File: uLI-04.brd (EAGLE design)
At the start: 57 x 38.5 mm, 38 parts, among them IC1 PIC18F14K50-I/SS, IC2 ADM2483, IC4 78L05F, J1 PICPROG2-V, J5 WEBP6-4, J6 WEBP6-4, J7 WEBP6-4, Q1 12.00 MHz, T1 IRF7306, X1 MINI-USB_SHIELD4P-USB-SPEC, X2 ARK1550/2_S

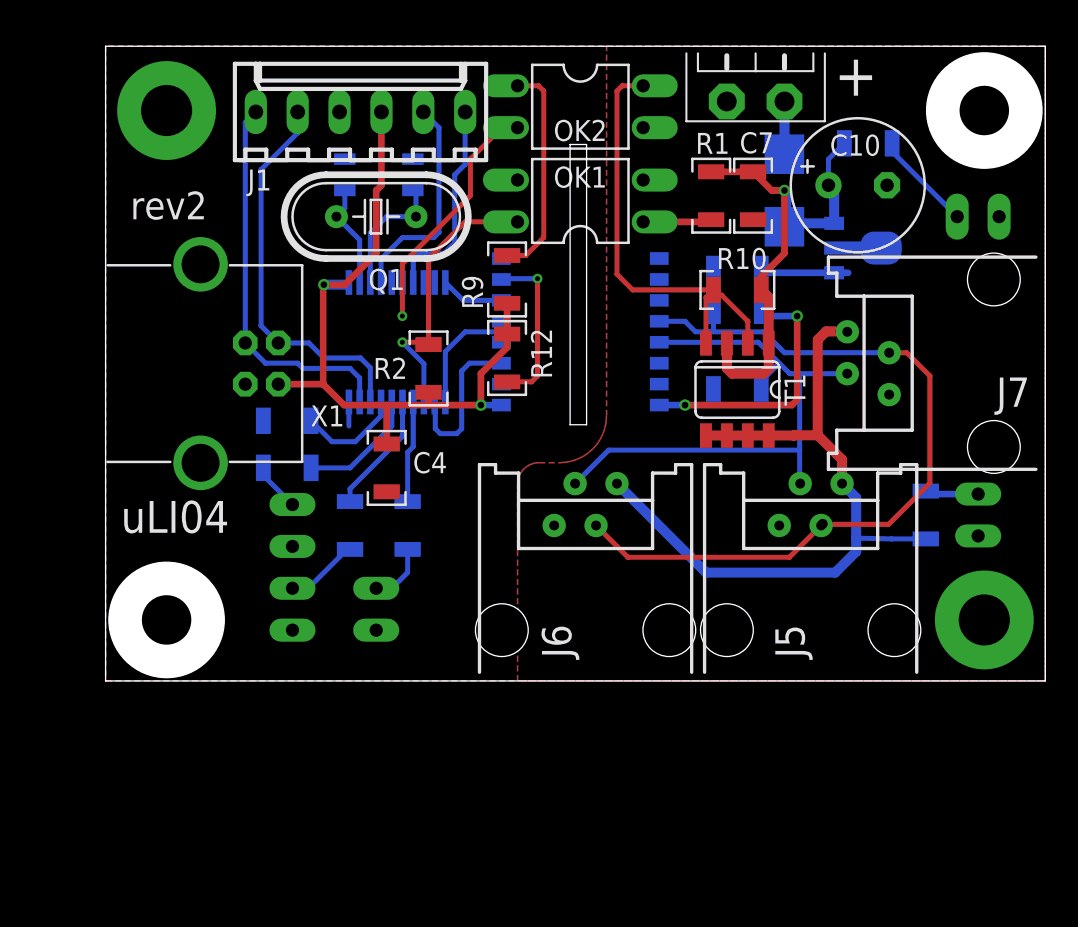
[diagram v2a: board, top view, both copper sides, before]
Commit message: Omezeni proudovych razu - schema
Pridan na schema rezistor a zmensen kondenzator pred stabilizator.
Editovano jen schema. Deska neupravena.
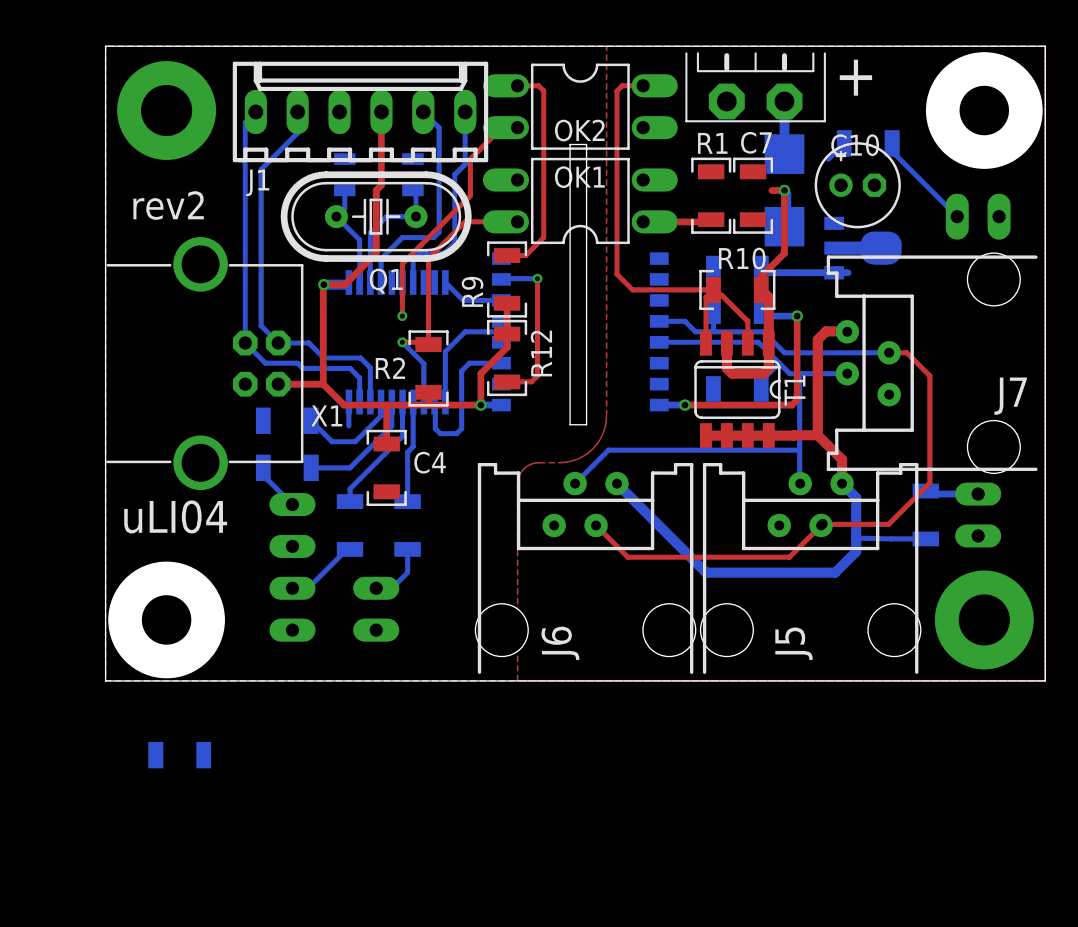
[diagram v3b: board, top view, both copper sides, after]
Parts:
- added R13: 22R, rcl:R1206
- C10: value 220u/35V -> 10u/35V; device rcl:E3,5-8 -> rcl:E2-5
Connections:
- new net N$10: C10.+, C7.1, IC4.3, R13.1
- net +12V: now also R13.2; no longer C10.+, C7.1, IC4.3
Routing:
- net +12V: track 31.4 -> 20.4 mm
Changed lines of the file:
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@@
 <grid distance="0.5" unitdist="mm" unit="mm" style="dots" multiple="2" display="no" altdistance="0.1" altunitdist="mm" altunit="mm"/>
 <layers>
-<layer number="1" name="Top" color="3" fill="1" visible="yes" active="yes"/>
+<layer number="1" name="Top" color="3" fill="1" visible="no" active="yes"/>
 <layer number="2" name="Route2" color="1" fill="3" visible="no" active="no"/>
 <layer number="3" name="Route3" color="4" fill="3" visible="no" active="no"/>
@@
 <layer number="19" name="Unrouted" color="6" fill="1" visible="yes" active="yes"/>
 <layer number="20" name="Dimension" color="15" fill="1" visible="yes" active="yes"/>
-<layer number="21" name="tPlace" color="7" fill="1" visible="yes" active="yes"/>
+<layer number="21" name="tPlace" color="7" fill="1" visible="no" active="yes"/>
 <layer number="22" name="bPlace" color="7" fill="1" visible="yes" active="yes"/>
-<layer number="23" name="tOrigins" color="15" fill="1" visible="yes" active="yes"/>
+<layer number="23" name="tOrigins" color="15" fill="1" visible="no" active="yes"/>
 <layer number="24" name="bOrigins" color="15" fill="1" visible="yes" active="yes"/>
 <layer number="25" name="tNames" color="7" fill="1" visible="no" active="yes"/>
@@
 <layer number="44" name="Drills" color="7" fill="1" visible="no" active="yes"/>
 <layer number="45" name="Holes" color="7" fill="1" visible="no" active="yes"/>
-<layer number="46" name="Milling" color="3" fill="1" visible="yes" active="yes"/>
+<layer number="46" name="Milling" color="3" fill="1" visible="no" active="yes"/>
 <layer number="47" name="Measures" color="7" fill="1" visible="no" active="yes"/>
 <layer number="48" name="Document" color="7" fill="1" visible="no" active="yes"/>
-<layer number="49" name="Reference" color="7" fill="1" visible="yes" active="yes"/>
+<layer number="49" name="Reference" color="7" fill="1" visible="no" active="yes"/>
 <layer number="50" name="dxf" color="7" fill="1" visible="no" active="no"/>
-<layer number="51" name="tDocu" color="7" fill="1" visible="yes" active="yes"/>
+<layer number="51" name="tDocu" color="7" fill="1" visible="no" active="yes"/>
 <layer number="52" name="bDocu" color="7" fill="1" visible="yes" active="yes"/>
 <layer number="53" name="tGND_GNDA" color="7" fill="9" visible="no" active="no"/>
@@
 <element name="R10" library="rcl" package="R1206" value="100k" x="40.3225" y="25.7175"/>
 <element name="T1" library="transistor-fet" package="SO08-IRF" value="IRF7306" x="40.3225" y="19.685" rot="R180"/>
-<element name="C10" library="rcl" package="E3,5-8" value="220u/35V" x="47.625" y="32.0675" smashed="yes">
+<element name="C10" library="rcl" package="E2-5" value="10u/35V" x="47.625" y="32.0675" smashed="yes">
 <attribute name="NAME" x="45.927" y="33.8615" size="1.27" layer="25" ratio="10"/>
 <attribute name="VALUE" x="45.339" y="34.0195" size="1.27" layer="27" ratio="10"/>
@@
 <attribute name="VALUE" x="28.8925" y="20.32" size="1.27" layer="27" font="vector" ratio="15" rot="R90"/>
 </element>
+<element name="R13" library="rcl" package="R1206" value="22R" x="6.5" y="-2.5" rot="MR180"/>
 </elements>
 <signals>
@@
 </signal>
 <signal name="+12V" class="1">
-<contactref element="IC4" pad="3"/>
-<contactref element="C7" pad="1"/>
 <contactref element="R1" pad="2"/>
 <contactref element="R8" pad="2"/>
@@
 <contactref element="T1" pad="3"/>
 <contactref element="T1" pad="1"/>
-<contactref element="C10" pad="+"/>
-<wire x1="46.1925" y1="29.7565" x2="43.3865" y2="29.7565" width="0.6096" layer="16"/>
 <wire x1="43.3865" y1="29.7565" x2="43.18" y2="29.55" width="0.6096" layer="16"/>
-<wire x1="46.1925" y1="29.7565" x2="46.1925" y2="31.722" width="0.6096" layer="16"/>
-<wire x1="46.1925" y1="31.722" x2="45.847" y2="32.0675" width="0.6096" layer="16"/>
 <wire x1="39.6875" y1="22.485" x2="39.6875" y2="20.955" width="0.6096" layer="1"/>
 <wire x1="39.6875" y1="20.955" x2="40.005" y2="20.6375" width="0.6096" layer="1"/>
@@
 <via x="43.18" y="31.75" extent="1-16" drill="0.4"/>
 <wire x1="43.18" y1="31.75" x2="42.4075" y2="31.75" width="0.4064" layer="1"/>
-<wire x1="42.4075" y1="31.75" x2="41.275" y2="32.8825" width="0.4064" layer="1"/>
 <wire x1="41.7725" y1="25.7175" x2="41.7725" y2="26.5325" width="0.4064" layer="1"/>
 <wire x1="41.7725" y1="26.5325" x2="43.18" y2="27.94" width="0.4064" layer="1"/>
 <wire x1="43.18" y1="27.94" x2="43.18" y2="31.75" width="0.4064" layer="1"/>
-<wire x1="38.735" y1="32.8825" x2="41.275" y2="32.8825" width="0.4064" layer="1"/>
-<wire x1="45.847" y1="32.0675" x2="45.847" y2="33.6445" width="0.3048" layer="16"/>
 <wire x1="45.847" y1="33.6445" x2="46.81" y2="34.6075" width="0.3048" layer="16"/>
+<contactref element="R13" pad="2"/>
+<wire x1="43.3865" y1="31.5435" x2="45.847" y2="33.6445" width="0" layer="19" extent="16-16"/>
+<wire x1="38.735" y1="32.8825" x2="42.4075" y2="31.75" width="0" layer="19" extent="1-1"/>
+<wire x1="7.95" y1="-2.5" x2="39.6875" y2="20.955" width="0" layer="19" extent="1-16"/>
 </signal>
 <signal name="XTAL2">
@@
 <wire x1="22" y1="18.8775" x2="21.96" y2="18.9175" width="0.3048" layer="16"/>
 </signal>
+<signal name="N$10" class="1">
+<contactref element="C10" pad="+"/>
+<contactref element="R13" pad="1"/>
+<contactref element="C7" pad="1"/>
+<contactref element="IC4" pad="3"/>
+<wire x1="46.1925" y1="29.7565" x2="46.609" y2="32.0675" width="0" layer="19" extent="16-16"/>
+<wire x1="41.275" y1="32.8825" x2="46.609" y2="32.0675" width="0" layer="19" extent="1-1"/>
+<wire x1="5.05" y1="-2.5" x2="41.275" y2="32.8825" width="0" layer="19" extent="1-16"/>
+</signal>
 </signals>

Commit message: Pridan brown-out reset pro PV pin
Jen schema.
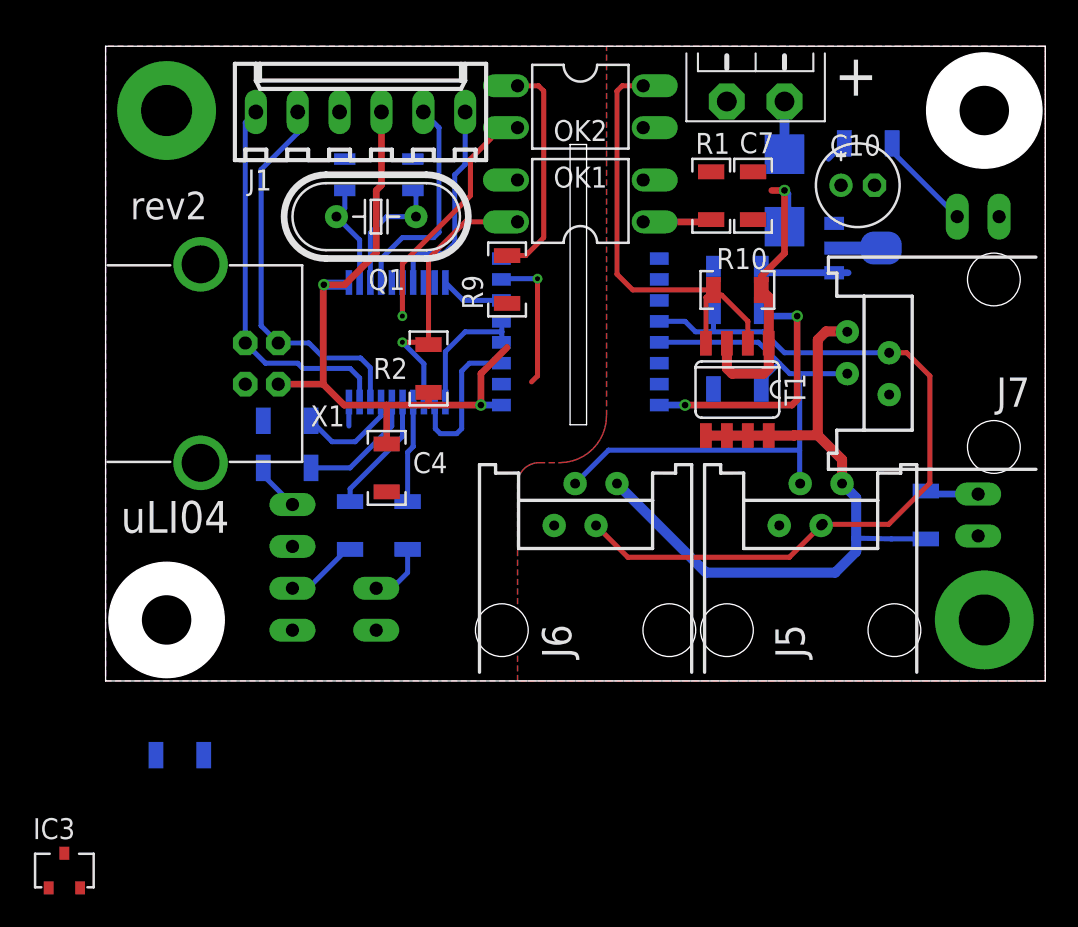
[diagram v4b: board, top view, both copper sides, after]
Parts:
- removed R12: OR, rcl:R1206
- added IC3: MCP130T, my:SOT23
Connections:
- removed net N$8: IC2.7, R12.1
- new net PV: IC2.7, IC3.1
- net GND: now also IC3.3
- net VDD: now also IC3.2; no longer R12.2
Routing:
- net N$8: track 10.1 -> 0.00 mm, vias 1 -> 0
- net PV: track 0.00 -> 8.62 mm, vias 0 -> 1
- net VDD: track 44.3 -> 41.6 mm
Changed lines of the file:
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@@
 <grid distance="0.5" unitdist="mm" unit="mm" style="dots" multiple="2" display="no" altdistance="0.1" altunitdist="mm" altunit="mm"/>
 <layers>
-<layer number="1" name="Top" color="3" fill="1" visible="no" active="yes"/>
+<layer number="1" name="Top" color="3" fill="1" visible="yes" active="yes"/>
 <layer number="2" name="Route2" color="1" fill="3" visible="no" active="no"/>
 <layer number="3" name="Route3" color="4" fill="3" visible="no" active="no"/>
@@
 <layer number="19" name="Unrouted" color="6" fill="1" visible="yes" active="yes"/>
 <layer number="20" name="Dimension" color="15" fill="1" visible="yes" active="yes"/>
-<layer number="21" name="tPlace" color="7" fill="1" visible="no" active="yes"/>
+<layer number="21" name="tPlace" color="7" fill="1" visible="yes" active="yes"/>
 <layer number="22" name="bPlace" color="7" fill="1" visible="yes" active="yes"/>
-<layer number="23" name="tOrigins" color="15" fill="1" visible="no" active="yes"/>
+<layer number="23" name="tOrigins" color="15" fill="1" visible="yes" active="yes"/>
 <layer number="24" name="bOrigins" color="15" fill="1" visible="yes" active="yes"/>
 <layer number="25" name="tNames" color="7" fill="1" visible="no" active="yes"/>
@@
 <layer number="44" name="Drills" color="7" fill="1" visible="no" active="yes"/>
 <layer number="45" name="Holes" color="7" fill="1" visible="no" active="yes"/>
-<layer number="46" name="Milling" color="3" fill="1" visible="no" active="yes"/>
+<layer number="46" name="Milling" color="3" fill="1" visible="yes" active="yes"/>
 <layer number="47" name="Measures" color="7" fill="1" visible="no" active="yes"/>
 <layer number="48" name="Document" color="7" fill="1" visible="no" active="yes"/>
-<layer number="49" name="Reference" color="7" fill="1" visible="no" active="yes"/>
+<layer number="49" name="Reference" color="7" fill="1" visible="yes" active="yes"/>
 <layer number="50" name="dxf" color="7" fill="1" visible="no" active="no"/>
-<layer number="51" name="tDocu" color="7" fill="1" visible="no" active="yes"/>
+<layer number="51" name="tDocu" color="7" fill="1" visible="yes" active="yes"/>
 <layer number="52" name="bDocu" color="7" fill="1" visible="yes" active="yes"/>
 <layer number="53" name="tGND_GNDA" color="7" fill="9" visible="no" active="no"/>
@@
 <attribute name="VALUE" x="50.2925" y="13.835" size="1.27" layer="28" font="vector" ratio="15" rot="MR270"/>
 </element>
-<element name="R12" library="rcl" package="R1206" value="OR" x="26.3525" y="21.59" smashed="yes" rot="R90">
-<attribute name="NAME" x="29.0825" y="20.32" size="1.27" layer="25" font="vector" ratio="15" rot="R90"/>
-<attribute name="VALUE" x="28.8925" y="20.32" size="1.27" layer="27" font="vector" ratio="15" rot="R90"/>
-</element>
 <element name="R13" library="rcl" package="R1206" value="22R" x="6.5" y="-2.5" rot="MR180"/>
+<element name="IC3" library="my" package="SOT23" value="MCP130T" x="-0.5" y="-9.5"/>
 </elements>
 <signals>
@@
 <contactref element="IC2" pad="8"/>
 <contactref element="IC2" pad="2"/>
+<contactref element="IC3" pad="3"/>
+<wire x1="13.335" y1="5.08" x2="-0.5" y2="-8.45" width="0" layer="19" extent="1-1"/>
 </signal>
 <signal name="VBUS">
@@
 <wire x1="26.3525" y1="22.225" x2="24.765" y2="20.6375" width="0.4064" layer="1"/>
 <wire x1="24.765" y1="20.6375" x2="24.765" y2="18.7325" width="0.4064" layer="1"/>
-<contactref element="R12" pad="2"/>
-<wire x1="26.3525" y1="22.225" x2="26.3525" y2="23.04" width="0.4064" layer="1"/>
-<wire x1="26.3525" y1="23.04" x2="26.3525" y2="24.9025" width="0.4064" layer="1"/>
 <contactref element="X1" pad="1"/>
 <wire x1="19.05" y1="18.7325" x2="16.4675" y2="18.7325" width="0.4064" layer="1"/>
@@
 <wire x1="15.2" y1="25.995" x2="15.24" y2="26.035" width="0.4064" layer="1"/>
 <wire x1="16.4675" y1="18.7325" x2="15.2" y2="20" width="0.4064" layer="1"/>
+<contactref element="IC3" pad="2"/>
+<wire x1="26.3525" y1="22.225" x2="26.3525" y2="24.9025" width="0" layer="19" extent="1-1"/>
+<wire x1="0.45" y1="-10.55" x2="19.05" y2="16.3725" width="0" layer="19" extent="1-1"/>
 </signal>
 <signal name="PROC_RX">
@@
 <wire x1="51.9325" y1="13.335" x2="54.9275" y2="13.335" width="0.4064" layer="16"/>
 </signal>
-<signal name="N$8">
-<contactref element="R12" pad="1"/>
+<signal name="PV">
 <contactref element="IC2" pad="7"/>
-<wire x1="26.3525" y1="20.14" x2="27.84" y2="20.14" width="0.3048" layer="1"/>
 <wire x1="27.84" y1="20.14" x2="28.2" y2="20.5" width="0.3048" layer="1"/>
 <wire x1="28.2" y1="20.5" x2="28.2" y2="26.4" width="0.3048" layer="1"/>
@@
 <wire x1="28.2" y1="26.4" x2="26.0571" y2="26.4" width="0.3048" layer="16"/>
 <wire x1="26.0571" y1="26.4" x2="26.0096" y2="26.3525" width="0.3048" layer="16"/>
+<contactref element="IC3" pad="1"/>
+<wire x1="-1.45" y1="-10.55" x2="27.84" y2="20.14" width="0" layer="19" extent="1-1"/>
 </signal>
 <signal name="N$5">
